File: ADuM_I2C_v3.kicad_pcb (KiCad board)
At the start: 4 copper layers, 25 x 12.5 mm, 42 parts, among them J1 A, J2 B, Q1 BSS138, Q2 BSS138, Q3 BSS138, Q4 BSS138, Q5 BSS138, Q6 BSS138, Q7 BSS138, Q8 BSS138, U1 ADuM1251ARZ, U2 ADuM1201AR

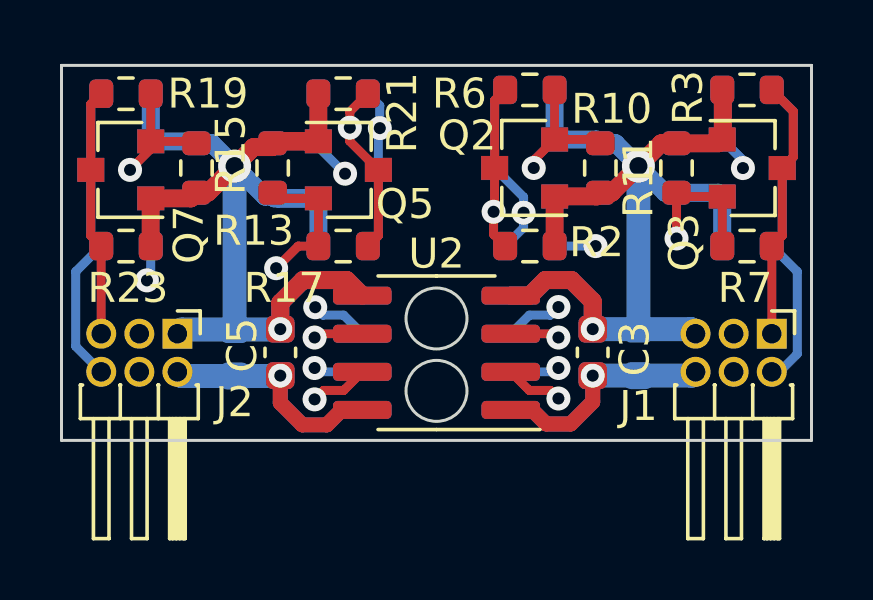
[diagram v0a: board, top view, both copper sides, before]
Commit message: Сформирован перечень элементов, 3D-модель, исправлены ошибки, реализована панелизация платы.
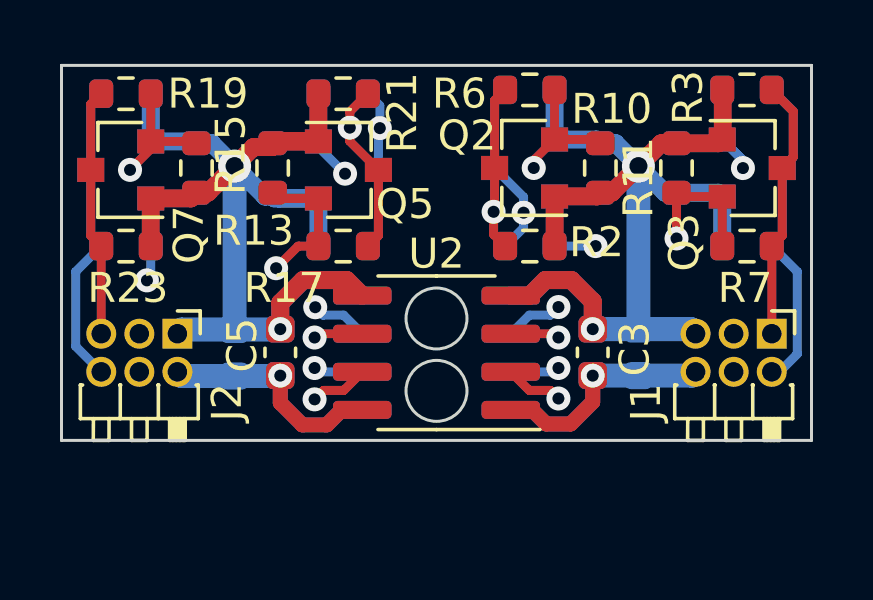
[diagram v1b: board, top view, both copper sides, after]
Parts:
- J1, J2: footprint Connector_PinHeader_1.27mm:PinHeader_2x03_P1.27mm_Horizontal -> Modules:PinHeader_2x03_P1.27mm_Horizontal_short

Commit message: Добавил изолирующие отверстия на схему. Подправил компоненты отверстий. Удалил контуры отверстий на обеих слоях платы. Обновил гербера и 3D-модель (step-файл).
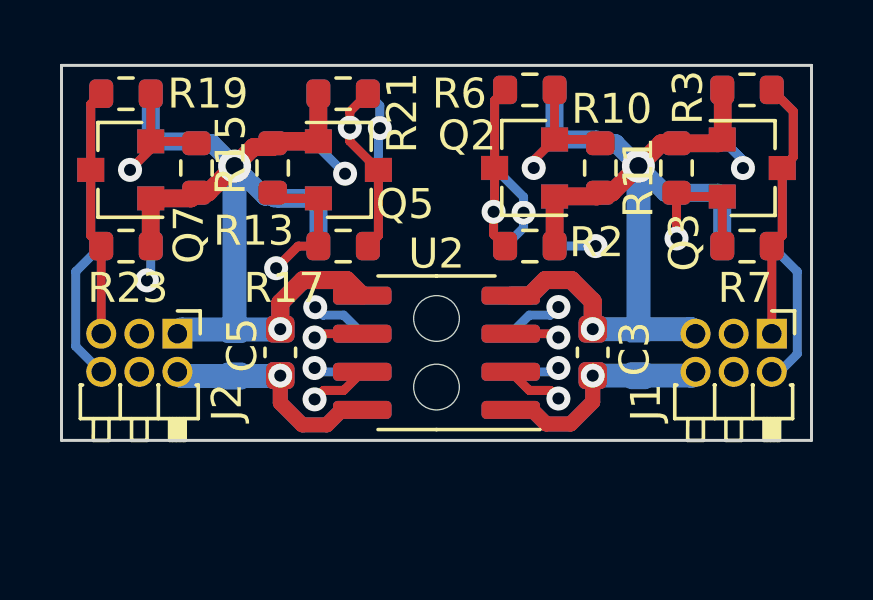
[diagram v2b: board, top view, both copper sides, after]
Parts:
- added H1: MountingHole_D1.524mm, Modules:MountingHole_D1.524mm, F.Cu at (100.0, 95.9)
- added H2: MountingHole_D1.524mm, Modules:MountingHole_D1.524mm, F.Cu at (100.0, 98.2)
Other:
- outline, holes or cut-outs redrawn
